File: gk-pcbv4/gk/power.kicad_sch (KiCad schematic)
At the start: 37 parts, among them J1 Conn_01x02, J2 Conn_01x02, U1 STPMIC25B JC Module, U2 BQ24075RGT (_not_ BQ24075*T*R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, U3 MAX17048, U4 INA236[AB]IDDFR

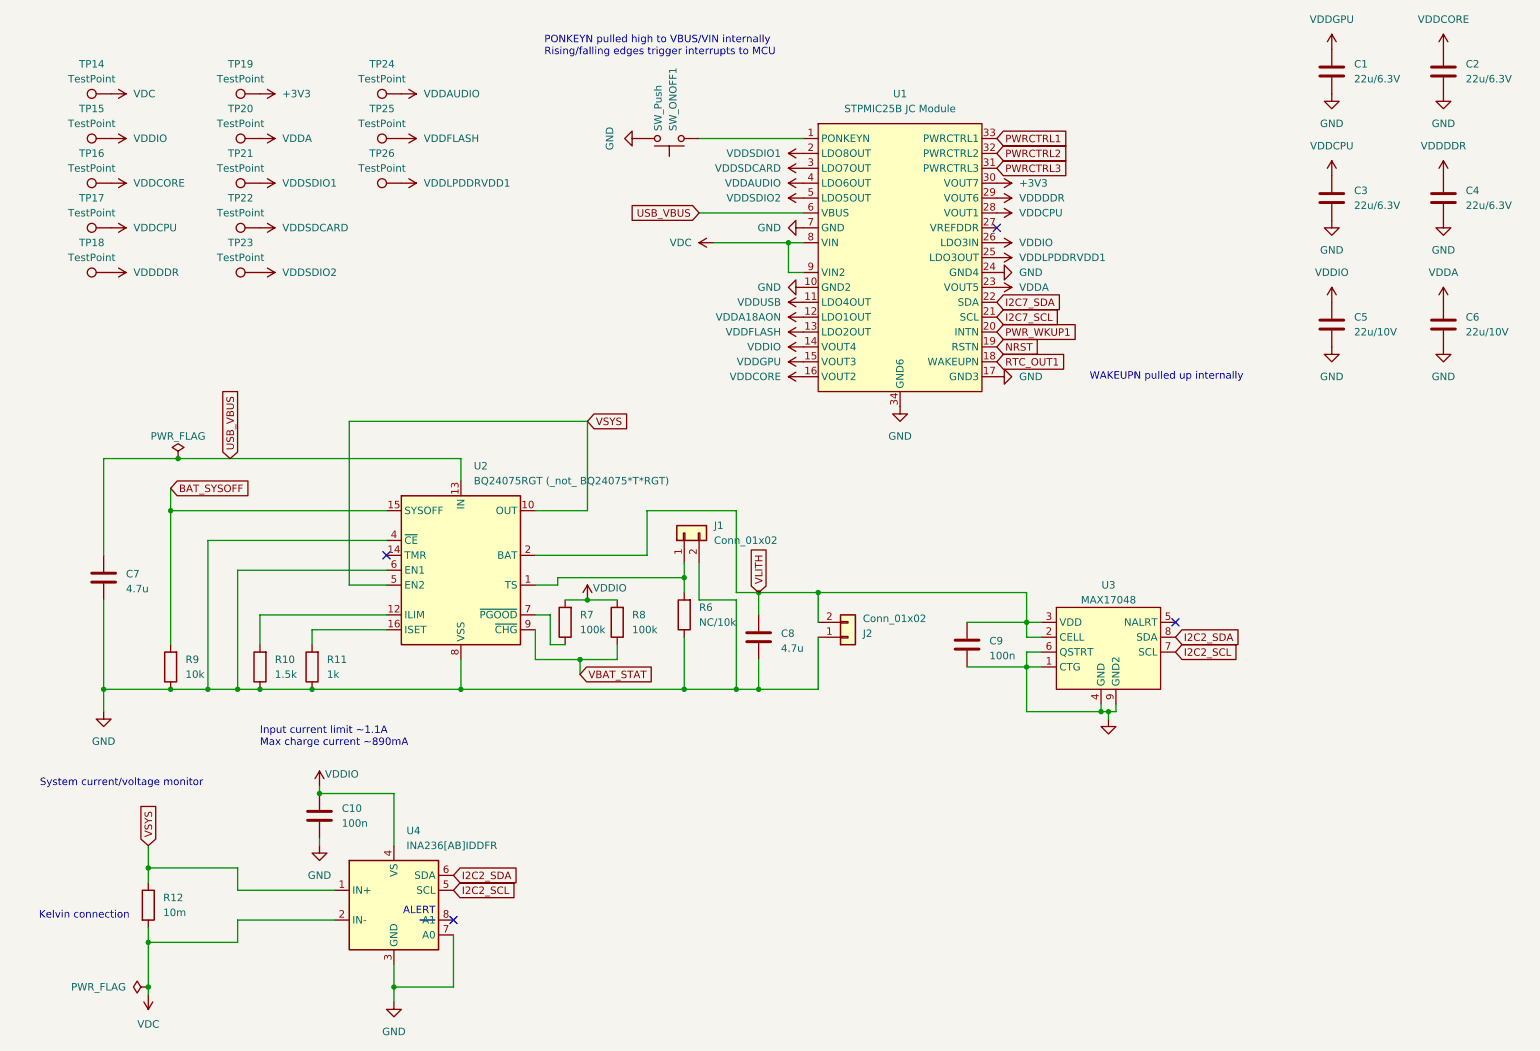
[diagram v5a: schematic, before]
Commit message: add bq25601 battery charger as alternative
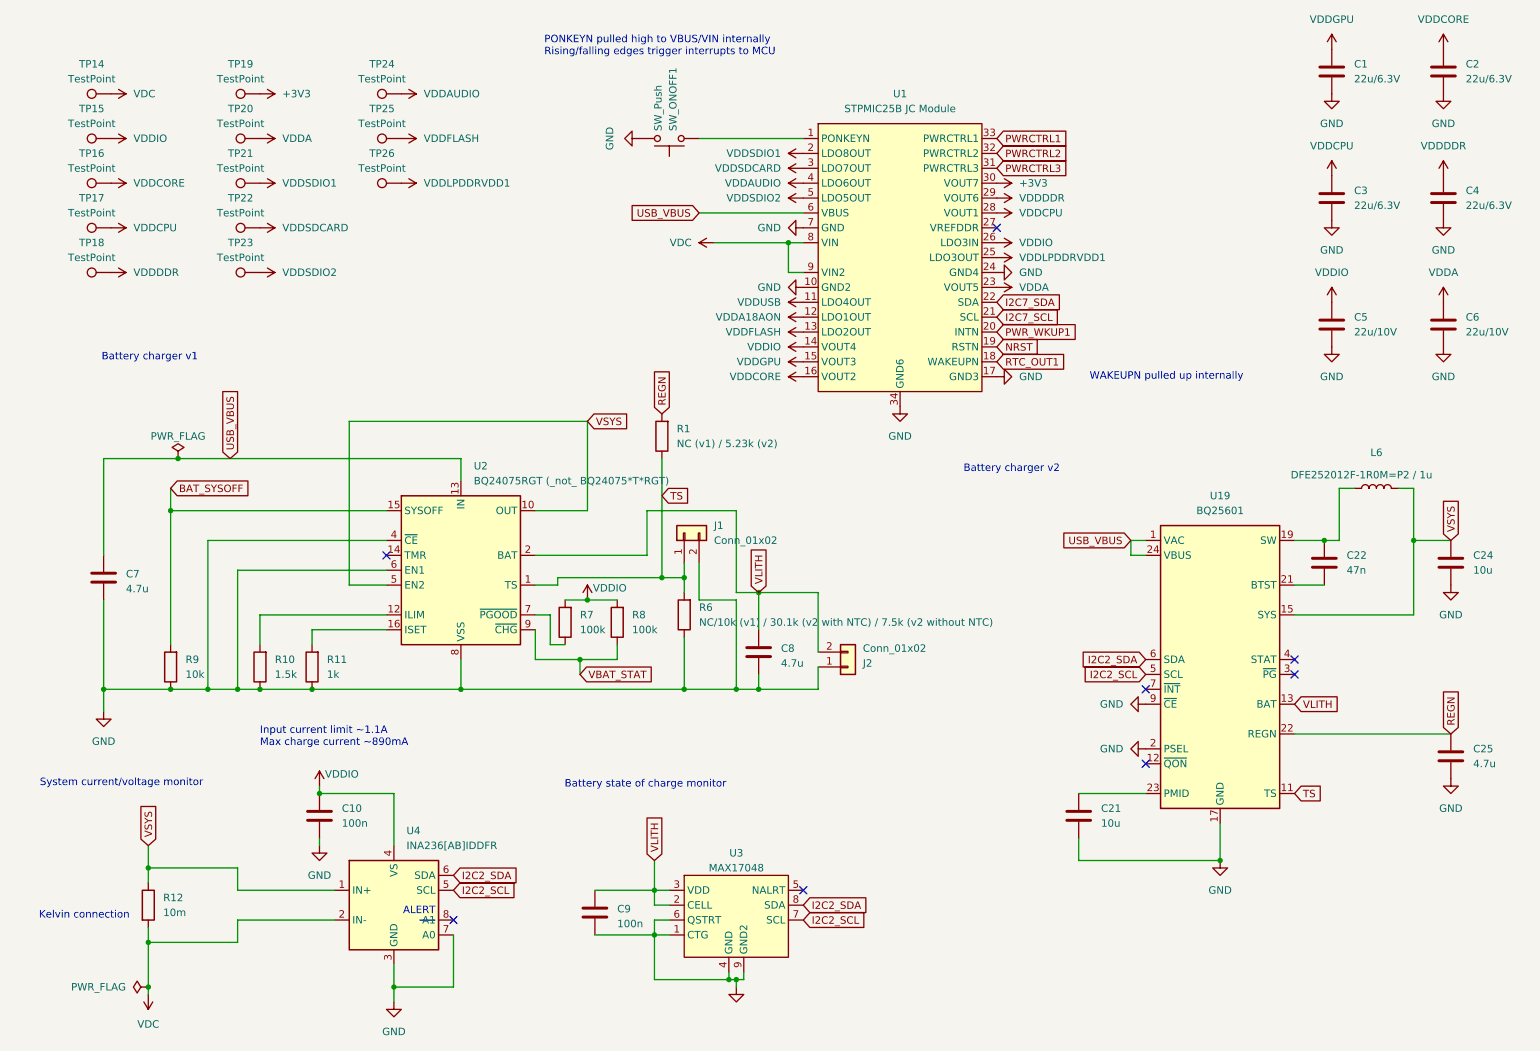
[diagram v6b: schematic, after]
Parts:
- added C21, C24: 10u, Capacitor_SMD:C_0805_2012Metric, symbol Device:C
- added C22: 47n, Capacitor_SMD:C_0603_1608Metric, symbol Device:C
- added C25: 4.7u, Capacitor_SMD:C_0805_2012Metric, symbol Device:C
- added L6: DFE252012F-1R0M=P2 / 1u, Inductor_SMD:L_1008_2520Metric, symbol Device:L
- added R1: NC (v1) / 5.23k (v2), Resistor_SMD:R_0603_1608Metric, symbol Device:R
- added U19: BQ25601, Package_DFN_QFN:Texas_RTW_WQFN-24-1EP_4x4mm_P0.5mm_EP2.7x2.7mm_ThermalVias, symbol Battery_Management:BQ25601
- R6: value NC/10k -> NC/10k (v1) / 30.1k (v2 with NTC) / 7.5k (v2 without NTC)
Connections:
- net GND: now also C21.2, C24.2, C25.2, U19.17 (GND), U19.18 (GND), U19.2 (PSEL), U19.25 (GND), U19.9 (~{CE})
- net I2C2_SCL: now also U19.5 (SCL)
- net I2C2_SDA: now also U19.6 (SDA)
- net USB_VBUS: now also U19.1 (VAC), U19.24 (VBUS)
- net VLITH: now also U19.13 (BAT), U19.14 (BAT)
- net VSYS: now also C24.1, L6.2, U19.15 (SYS), U19.16 (SYS)
- net TS: now reaches J1.1 (Pin_1), R6.2, U2.1 (TS)
- net TS: now also R1.1, U19.11 (TS)
- new net: C22.1, L6.1, U19.19 (SW), U19.20 (SW)
- new net: C22.2, U19.21 (BTST)
- new net: C21.1, U19.23 (PMID)
- new net REGN: C25.1, R1.2, U19.22 (REGN)
- no-connect marks 4 -> 8
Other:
- note added: "Battery charger v1"
- note added: "Battery charger v2"
- note added: "Battery state of charge monitor"
- moved on the sheet: C8, C9, J2, U3

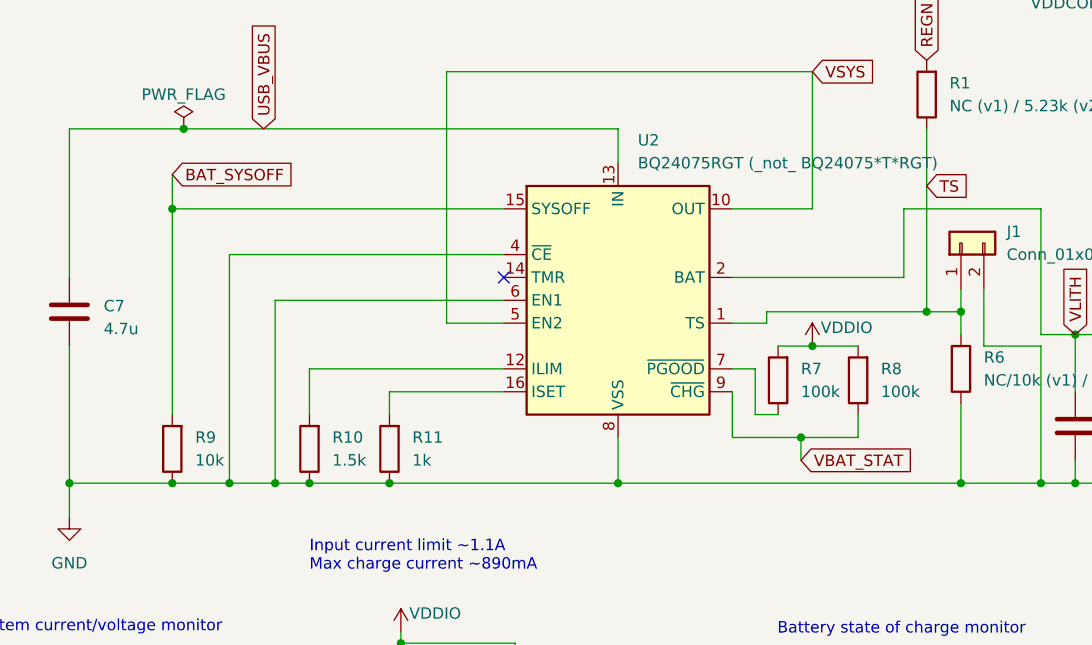
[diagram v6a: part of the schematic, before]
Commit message: update pcb routing based on new v2 changes
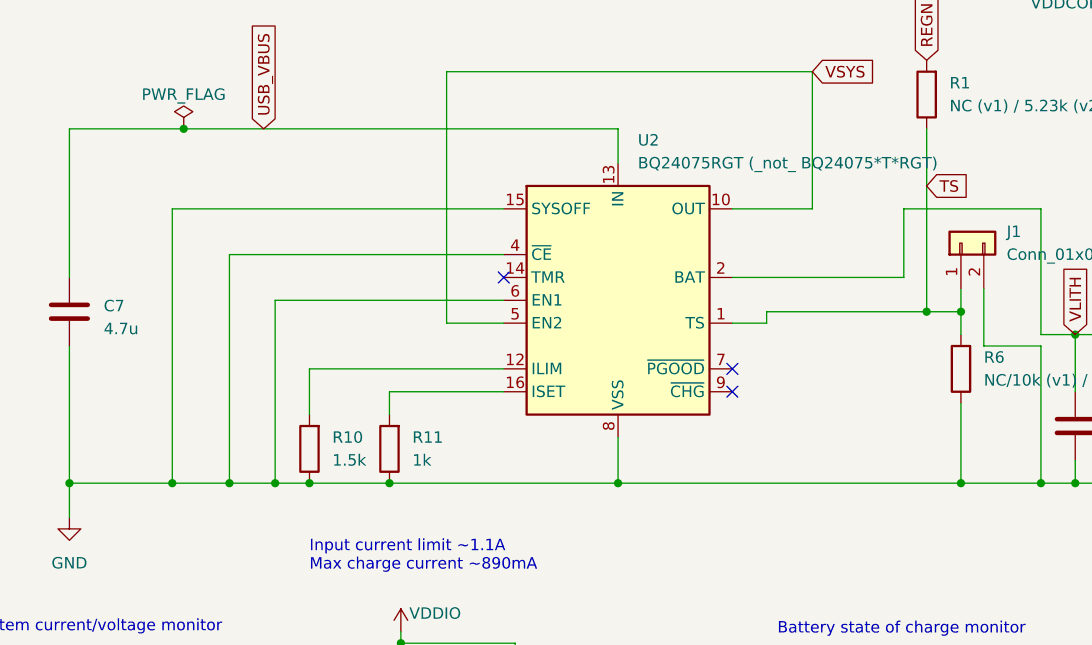
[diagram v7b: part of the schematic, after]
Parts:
- removed R7, R8: 100k, Resistor_SMD:R_0603_1608Metric, symbol Device:R
- removed R9: 10k, Resistor_SMD:R_0603_1608Metric, symbol Device:R
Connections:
- net BAT_SYSOFF is gone; now on net GND: U2.15 (SYSOFF)
- net VBAT_STAT: no longer names the net of U2.9 (~{CHG})
- no-connect marks 8 -> 10
